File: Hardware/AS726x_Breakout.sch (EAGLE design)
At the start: 25 parts, among them J2 Serial Interface, U1 AS726X, U3 4MB Flash

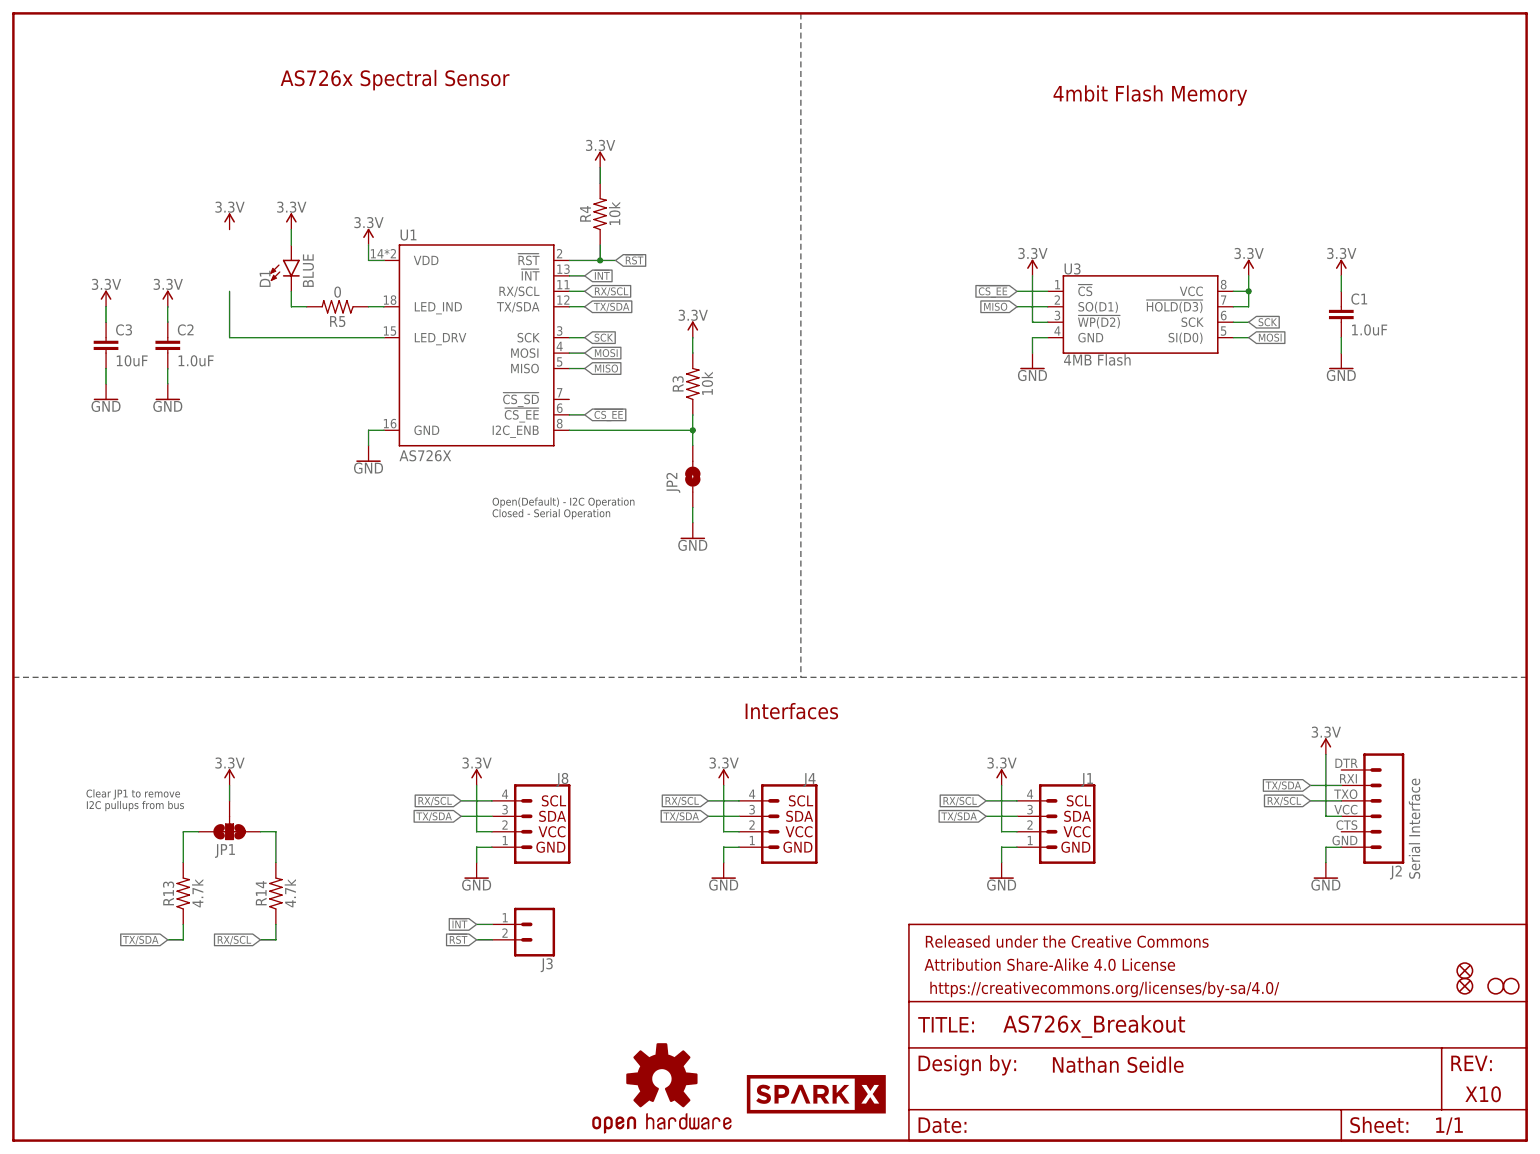
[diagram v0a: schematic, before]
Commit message: Adding firmware, panel, and small fix to dimension on main layout.
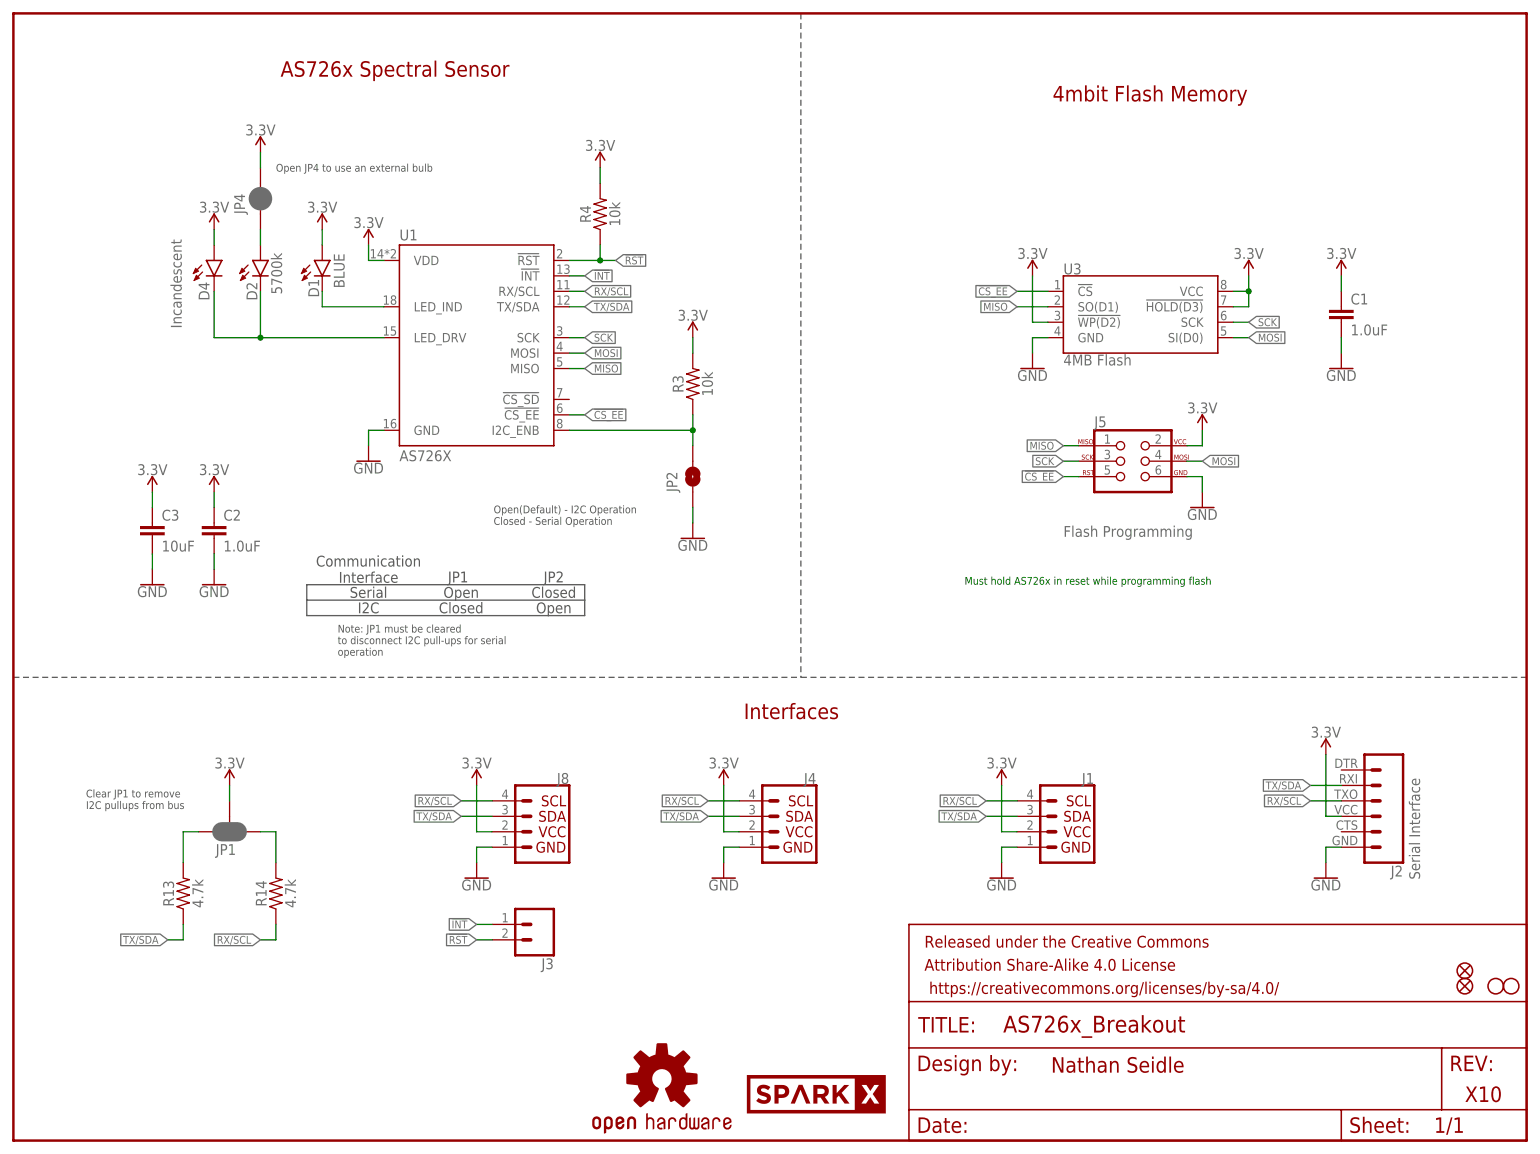
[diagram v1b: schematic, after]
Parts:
- removed R5: 0, SparkFun-Resistors:0OHM-0603-1/10W-5%
- added D2: 5700k, SparkX:LEDLD
- added D4: Incandescent, SparkX:LEDNS
- added J5: Flash Programming, SparkFun-Connectors:AVR_SPI_PROG_3X2TESTPOINTS
- added JP4: JUMPER-SMT_2_NC_PASTE_NO-SILK, SparkFun-Jumpers:JUMPER-SMT_2_NC_PASTE_NO-SILK
- JP1: value JUMPER-SMT_3_2-NC_TRACE_SILK -> JUMPER-SMT_3_2-NC_PASTE_SILK; device SparkFun-Jumpers:JUMPER-SMT_3_2-NC_TRACE_SILK -> SparkFun-Jumpers:JUMPER-SMT_3_2-NC_PASTE_SILK
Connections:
- removed net N$3: D1.C, R5.2
- new net LED_DRV: D2.C, D4.C, U1.LED_DRV
- net !CS_EE: now also J5.5
- net 3.3V: now also D4.A, J5.2, JP4.2
- net GND: now also J5.6
- net MISO: now also J5.1
- net MOSI: now also J5.4
- net N$2: now also D1.C; no longer R5.1
- net N$6: now also D2.A, JP4.1; no longer U1.LED_DRV
- net SCK: now also J5.3
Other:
- note added: "Closed"
- note added: "Communication Interface"
- note added: "I2C"
- note added: "JP1"
- note added: "JP2"
- note added: "Must hold AS726x in reset while programming flash"
- note added: "Note: JP1 must be cleared to disconnect I2C pull-ups for serial operation"
- note added: "Open"
- note added: "Open JP4 to use an external bulb"
- note added: "Serial"
- moved on the sheet: C2, C3, D1

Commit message: Examples are fully functional
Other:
- note added: "Communication Protocol"
- note added: "Note: for serial operation JP1 must be cleared to disconnect I2C pull-ups"
- note added: "The AS726x must be held in reset while programming flash"
- note removed: "Communication Interface"
- note removed: "Must hold AS726x in reset while programming flash"
- note removed: "Note: JP1 must be cleared to disconnect I2C pull-ups for serial operation"
- moved on the sheet: C1, J5, U3
